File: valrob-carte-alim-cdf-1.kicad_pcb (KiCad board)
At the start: 4 copper layers, 87 x 57 mm, 201 parts, among them J1 USB_C_Receptacle_USB2.0_14P, J10 Conn_01x02, J11 Conn_01x02, J12 Conn_01x02, J13 Conn_01x02, J14 Conn_01x02, J15 Conn_01x02, J16 Conn_01x02, J17 Conn_01x02, J18 Conn_01x02, J19 Conn_01x02, J2 Conn_01x02, J20 Conn_01x02, J21 Conn_01x02, J22 Conn_01x02, J3 Conn_01x04_Pin, J4 Conn_01x02, J5 Conn_01x02, J6 Conn_01x02, J7 Conn_01x02, J8 Conn_01x02, J9 Conn_01x02, SW1 SW_Push, SW2 SW_Push, SW3 SW_Push, U1 SN65HVD230, U10 TPS259472A, U11 TPS259472A, U12 TPS259472A, U2 ESP32-S3-WROOM-1, U3 TLV75733PDBV, U4 TPS56A37, U5 TPS56A37, U6 TPS259472A, U7 TPS259472A, U8 TPS259472A, U9 TPS259472A

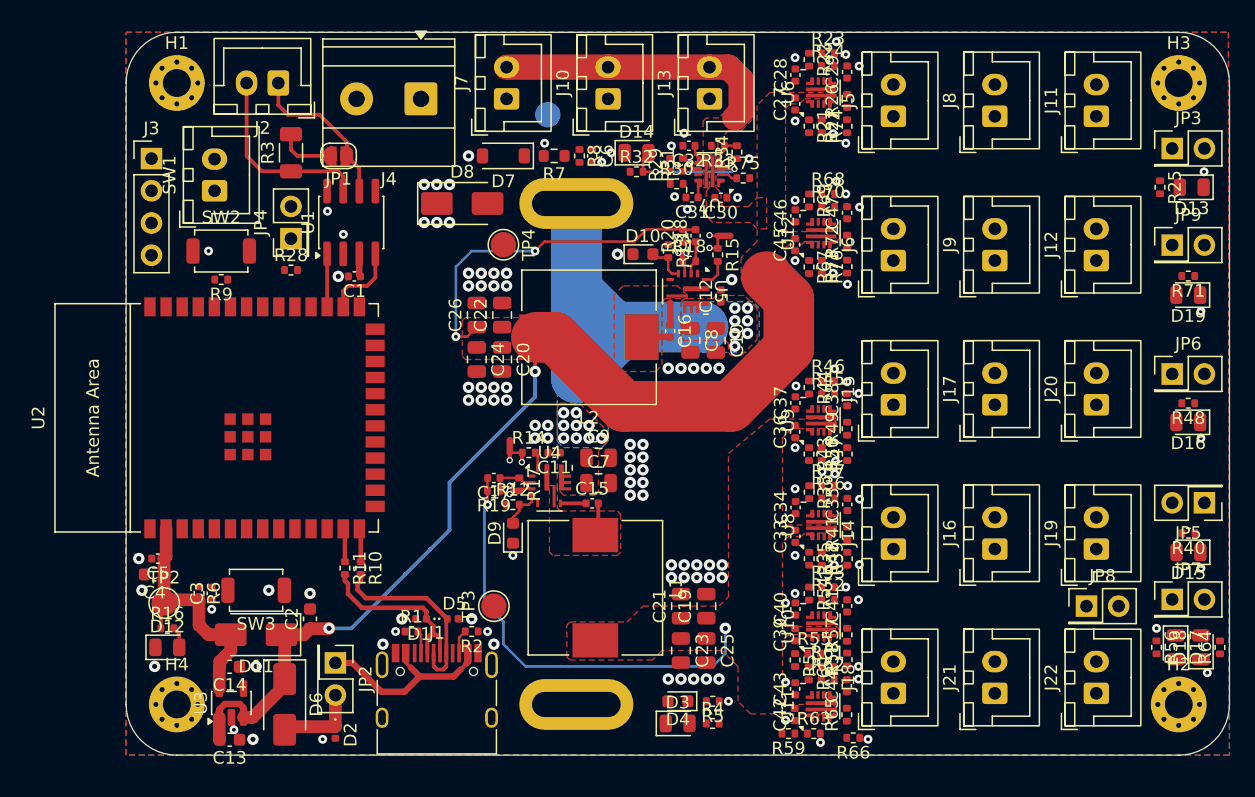
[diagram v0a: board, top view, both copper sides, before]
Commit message: pcb: add local efuse routing
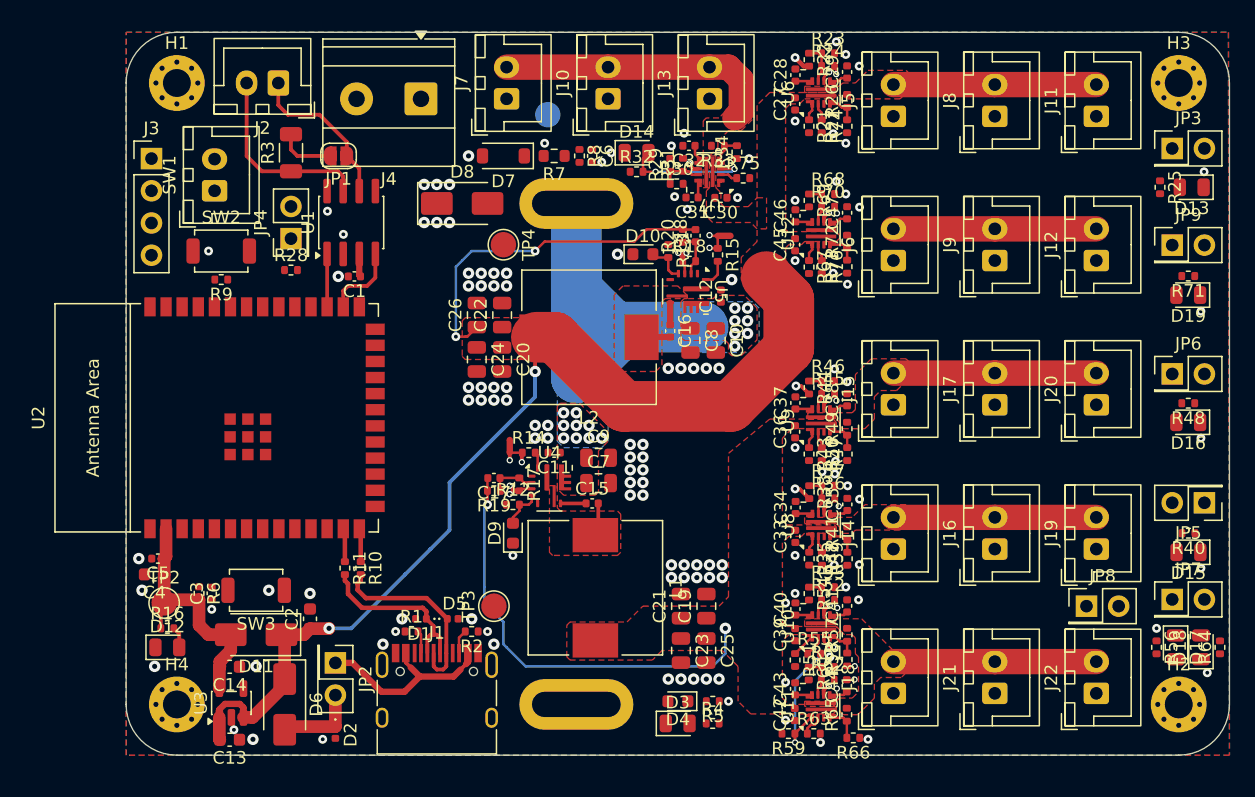
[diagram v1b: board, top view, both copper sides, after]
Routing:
- net /Connectors/Efuse 5V 5A 2/OUT: track 0.00 -> 16.0 mm
- net /Connectors/Efuse 5V 5A 1/OUT: track 0.00 -> 16.0 mm
- net /Connectors/Efuse 12V 5A 3/OUT: track 0.00 -> 16.0 mm
- net /Connectors/Efuse 12V 5A 2/OUT: track 0.00 -> 16.0 mm
- net /Connectors/Efuse 12V 5A 1/OUT: track 0.00 -> 16.0 mm
- net PG_12V_3: track 0.00 -> 12.7 mm, vias 0 -> 2
- net GND: track 0.95 -> 11.3 mm, vias 135 -> 147
- net ILM_5V_1: track 0.00 -> 3.29 mm
- net ILM_12V_2: track 0.00 -> 3.29 mm
- net ILM_5V_2: track 0.00 -> 3.29 mm
- net ILM_12V_3: track 0.00 -> 3.29 mm
- net ILM_12V_4: track 0.00 -> 3.29 mm
- net ILM_5V_3: track 0.00 -> 3.29 mm
- net ILM_12V_1: track 0.00 -> 3.29 mm
- net Net-(U11-PGTH): track 0.00 -> 2.78 mm
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- added copper zone on F.Cu, net /Connectors/Efuse 12V 5A 1/OUT
- added copper zone on F.Cu, net /Connectors/Efuse 12V 5A 2/OUT
- added copper zone on F.Cu, net /Connectors/Efuse 12V 5A 3/OUT
- added copper zone on F.Cu, net /Connectors/Efuse 5V 5A 1/OUT

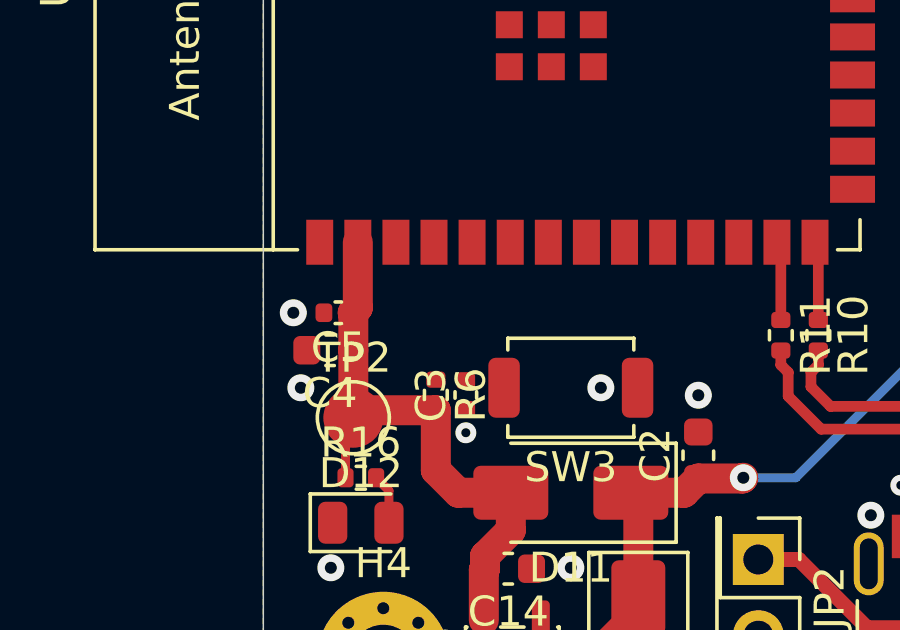
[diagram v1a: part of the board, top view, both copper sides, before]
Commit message: pcb: add CHIP_PU routing
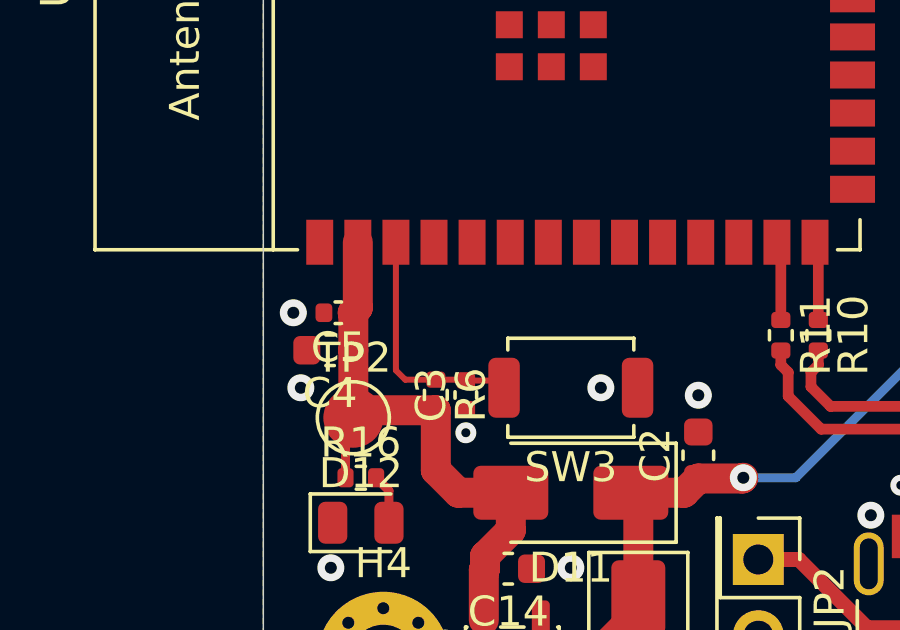
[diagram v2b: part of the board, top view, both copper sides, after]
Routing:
- net /CHIP_PU: track 0.00 -> 8.12 mm
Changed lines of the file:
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@@
+	)
+	(segment
+		(start 96.75 96.76)
+		(end 97.785 96.76)
+		(width 0.2)
+		(layer "F.Cu")
+		(net 5)
+	)
+	(segment
+		(start 94.73 96.73)
+		(end 94.42 96.42)
+		(width 0.2)
+		(layer "F.Cu")
+		(net 5)
+	)
+	(segment
+		(start 95.75 96.73)
+		(end 94.73 96.73)
+		(width 0.2)
+		(layer "F.Cu")
+		(net 5)
+	)
+	(segment
+		(start 96.72 96.73)
+		(end 96.75 96.76)
+		(width 0.2)
+		(layer "F.Cu")
+		(net 5)
+	)
+	(segment
+		(start 95.75 96.73)
+		(end 96.72 96.73)
+		(width 0.2)
+		(layer "F.Cu")
+		(net 5)
+	)
+	(segment
+		(start 97.785 96.76)
+		(end 98.025 97)
+		(width 0.2)
+		(layer "F.Cu")
+		(net 5)
+	)
+	(segment
+		(start 94.42 96.42)
+		(end 94.42 92.15)
+		(width 0.2)
+		(layer "F.Cu")
+		(net 5)
 	)
 	(segment

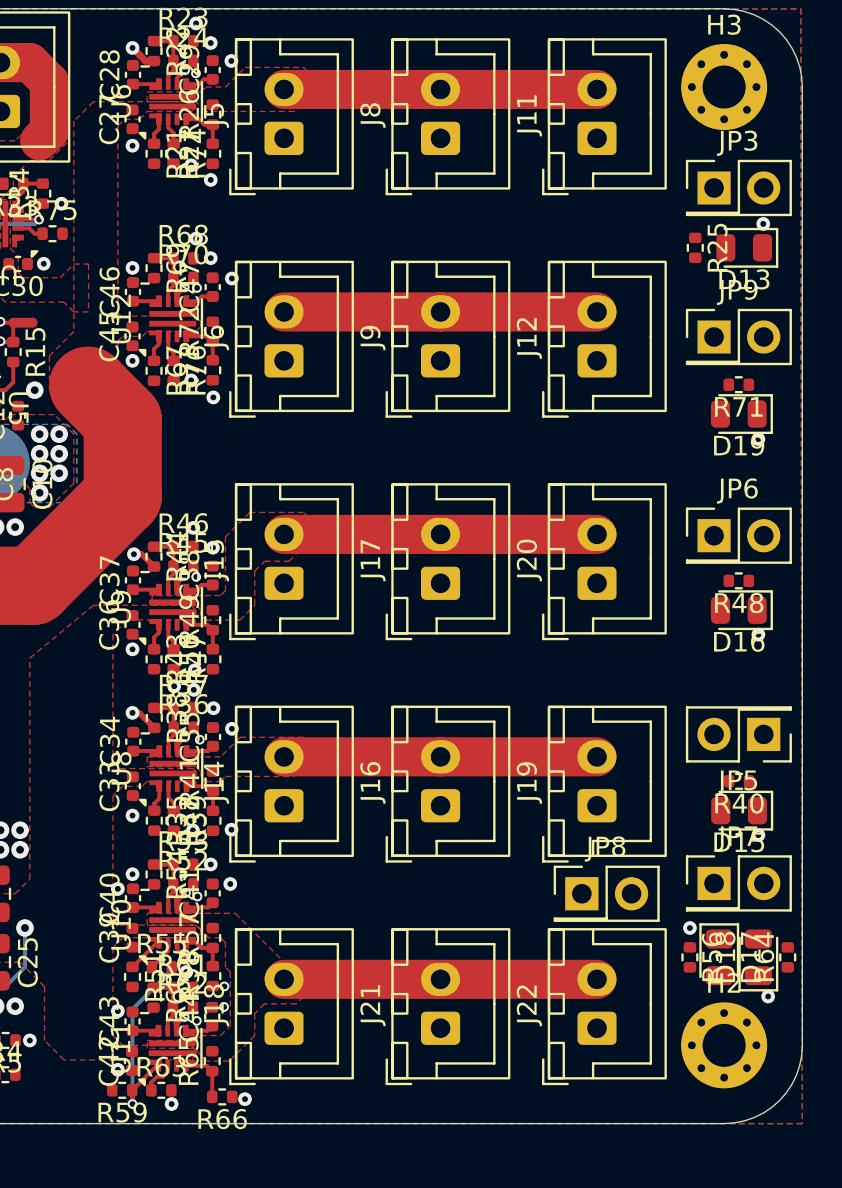
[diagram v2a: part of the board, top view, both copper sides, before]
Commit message: pcb: add efuses' PG leds and en jumpers routing
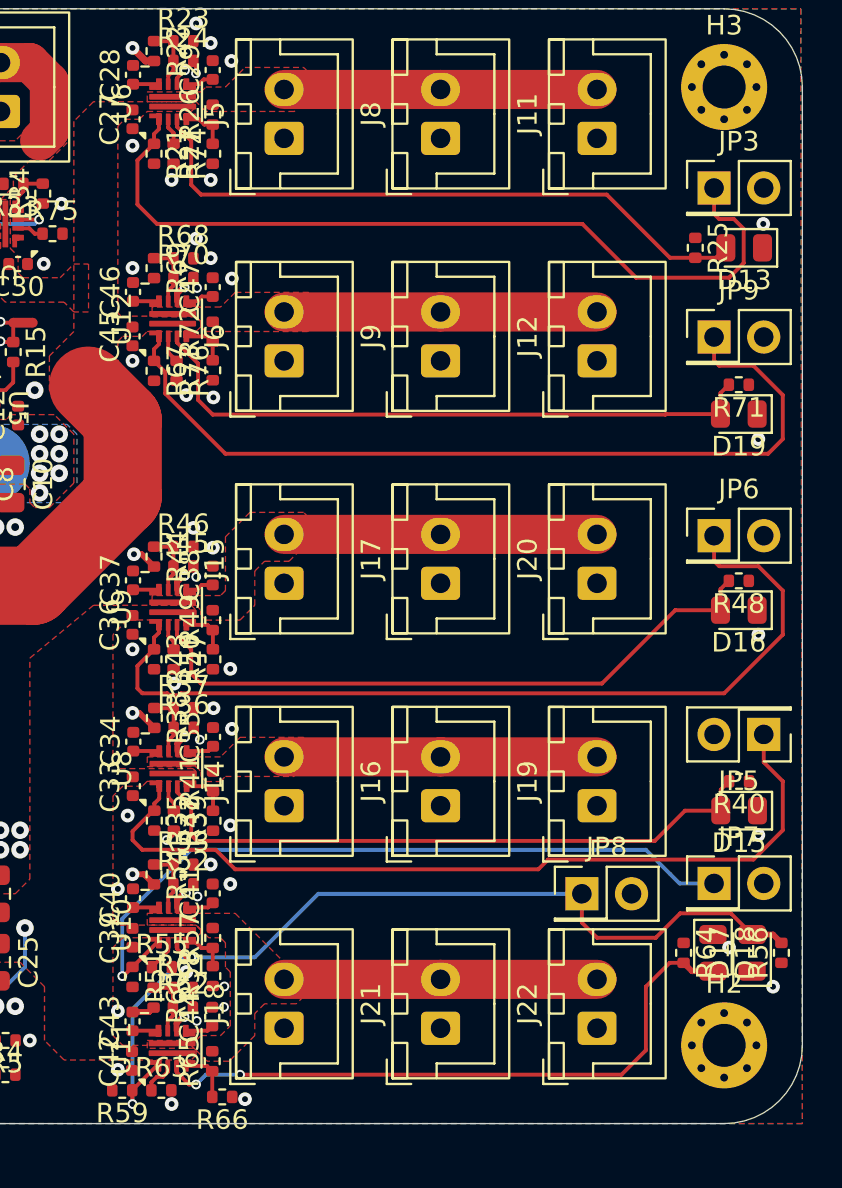
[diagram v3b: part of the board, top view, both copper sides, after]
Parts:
- moved R64 5.33 mm to (170.9, 101.3), turned to -90 degrees
- moved R56 4.68 mm to (175.9, 101.3), turned to 90 degrees
- moved D18 2.33 mm to (172.4, 101.3), turned to -90 degrees
- moved D17 1.69 mm to (174.4, 101.3), turned to 90 degrees
- moved R76 0.15 mm to (145.0, 71.5)
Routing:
- net EN_12V_2: track 1.35 -> 45.8 mm
- net EN_5V_2: track 1.35 -> 44.1 mm
- net EN_12V_1: track 1.35 -> 43.4 mm
- net EN_5V_1: track 1.35 -> 42.6 mm
- net EN_12V_3: track 1.86 -> 38.0 mm, vias 0 -> 1
- net PG_12V_3: track 12.7 -> 47.2 mm
- net PG_12V_2: track 0.00 -> 33.3 mm
- net PG_5V_1: track 0.00 -> 32.7 mm
- net PG_12V_4: track 0.00 -> 32.7 mm, vias 0 -> 2
- net PG_5V_2: track 0.00 -> 32.4 mm
- net PG_12V_1: track 0.00 -> 32.3 mm
- net GND: track 11.3 -> 14.4 mm, vias 147 -> 146
- added copper zone on F.Cu, net /Connectors/Efuse 5V 5A 2/OUT

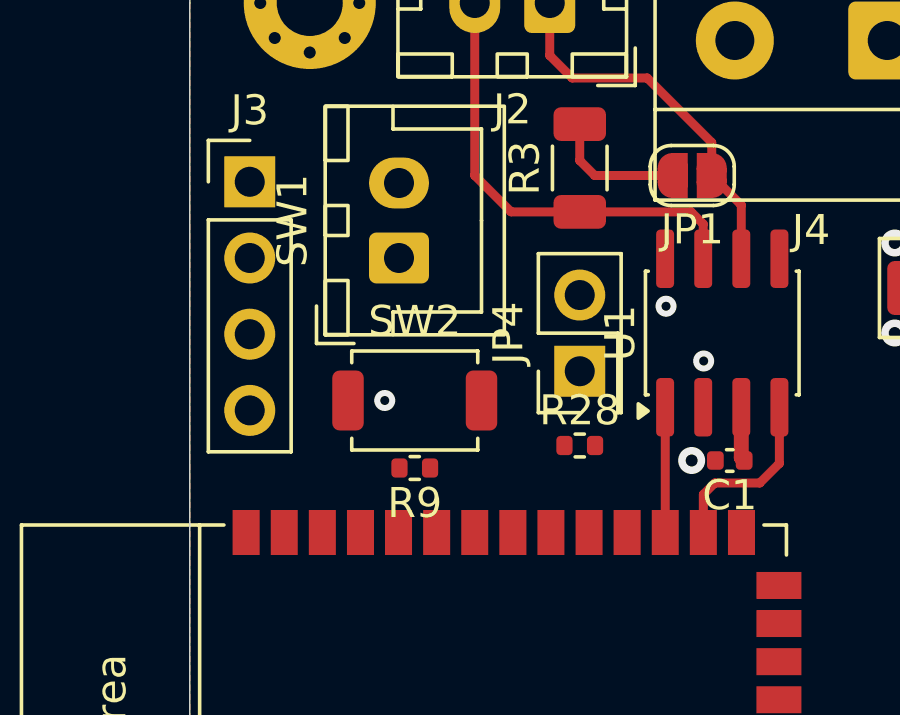
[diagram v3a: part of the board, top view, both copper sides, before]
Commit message: pcb: add BAU routing
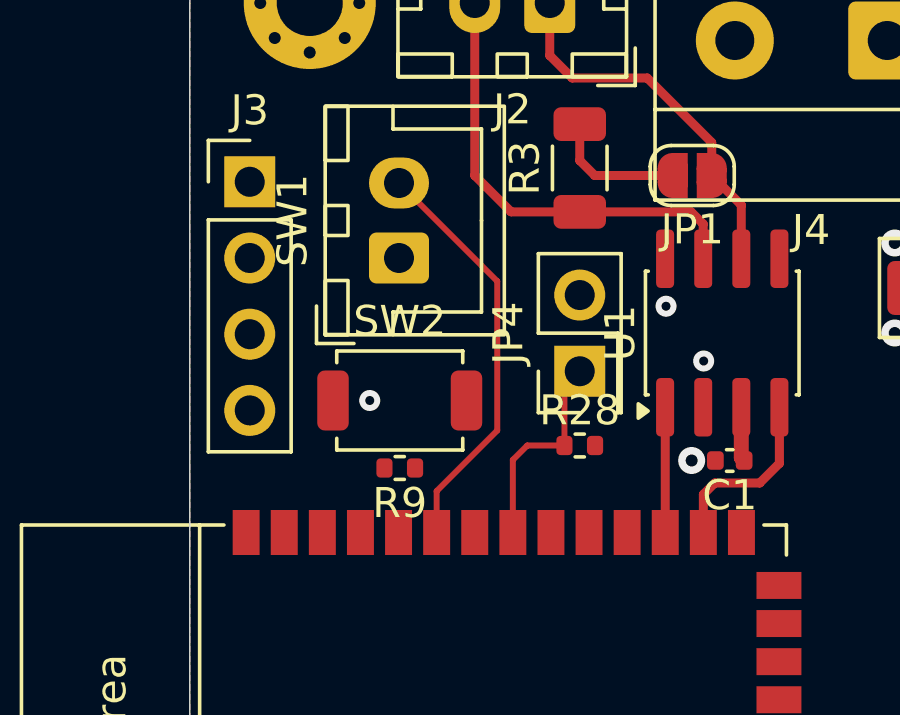
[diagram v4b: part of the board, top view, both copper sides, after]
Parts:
- moved R9 0.50 mm to (97.0, 72.5)
- moved SW2 0.50 mm to (97.0, 70.2)
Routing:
- net /BAU: track 0.00 -> 13.8 mm
- net EN_5V_3: track 0.00 -> 7.03 mm
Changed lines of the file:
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@@
 	(footprint "Button_Switch_SMD:SW_SPST_TS-1088-xR020"
 		(layer "F.Cu")
-		(at 97.5 70.25)
+		(at 97 70.25)
 		(descr "SMD Tactile Switch, 3.9x3x2 mm, https://lcsc.com/datasheet/lcsc_datasheet_2504101957_XUNPU-TS-1088-AR02016_C720477.pdf")
 		(tags "Tactile Switch")
@@
 	(footprint "Resistor_SMD:R_0402_1005Metric"
 		(layer "F.Cu")
-		(at 97.5 72.5 180)
+		(at 97 72.5 180)
 		(descr "Resistor SMD 0402 (1005 Metric), square (rectangular) end terminal, IPC-7351 nominal, (Body size source: IPC-SM-782 page 72, https://www.pcb-3d.com/wordpress/wp-content/uploads/ipc-sm-782a_amendment_1_and_2.pdf), generated with kicad-footprint-generator")
 		(tags "resistor")
@@
 	)
 	(via
-		(at 96.5 70.25)
+		(at 96 70.25)
 		(size 0.7)
 		(drill 0.3)
@@
 	)
 	(segment
+		(start 101.25 71.75)
+		(end 102.49 71.75)
+		(width 0.2)
+		(layer "F.Cu")
+		(net 59)
+	)
+	(segment
+		(start 100.77 72.23)
+		(end 101.25 71.75)
+		(width 0.2)
+		(layer "F.Cu")
+		(net 59)
+	)
+	(segment
+		(start 100.77 74.65)
+		(end 100.77 72.23)
+		(width 0.2)
+		(layer "F.Cu")
+		(net 59)
+	)
+	(segment
+		(start 102.49 69.785)
+		(end 103 69.275)
+		(width 0.2)
+		(layer "F.Cu")
+		(net 59)
+	)
+	(segment
+		(start 102.49 71.75)
+		(end 102.49 69.785)
+		(width 0.2)
+		(layer "F.Cu")
+		(net 59)
+	)
+	(segment
 		(start 142.75 95.0575)
 		(end 143.8075 94)
@@
 	)
 	(segment
+		(start 98.23 74.65)
+		(end 98.23 73.27)
+		(width 0.2)
+		(layer "F.Cu")
+		(net 89)
+	)
+	(segment
+		(start 100.25 66.275)
+		(end 96.975 63)
+		(width 0.2)
+		(layer "F.Cu")
+		(net 89)
+	)
+	(segment
+		(start 98.23 73.27)
+		(end 100.25 71.25)
+		(width 0.2)
+		(layer "F.Cu")
+		(net 89)
+	)
+	(segment
+		(start 100.25 71.25)
+		(end 100.25 66.275)
+		(width 0.2)
+		(layer "F.Cu")
+		(net 89)
+	)
+	(segment
